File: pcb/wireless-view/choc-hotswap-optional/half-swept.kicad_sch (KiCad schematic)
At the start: 25 parts, among them J1 JST-BATTERY, SW1 SW_Push, SW10 SW_Push, SW11 SW_Push, SW12 SW_Push, SW13 SW_DPDT, SW14 SW_Push, SW15 SW_Push, SW16 SW_Push, SW17 SW_Push, SW18 SW_Push, SW2 SW_Push, SW20 SW_Push, SW21 SW_Push, SW3 SW_Push, SW4 SW_Push, SW5 SW_Push, SW6 SW_Push, SW7 SW_DPDT, SW8 SW_Push, SW9 SW_Push, U1 nice_nano

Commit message: updated wireless sweeeeeep to support mill-max as well
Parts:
- SW1, SW10, SW11, SW12, SW14, SW15, SW16, SW17, SW18, SW2, SW20, SW21, SW3, SW4, SW5, SW6, SW8, SW9: footprint fingerpunch:Kailh_socket_PG1350_optional_reversible -> fingerpunch:Kailh_socket_PG1350_optional_reversible_millmax

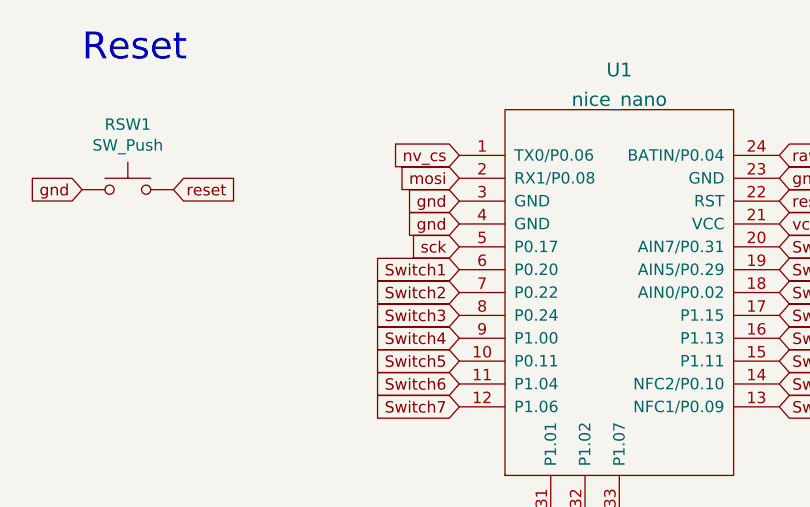
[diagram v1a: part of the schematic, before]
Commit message: Change n!n pin assigmnets to match ZMK's nice_view_adapter
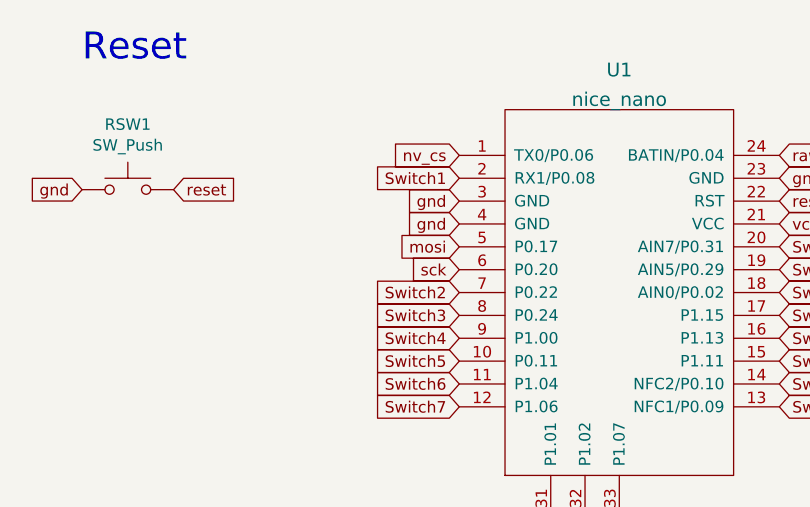
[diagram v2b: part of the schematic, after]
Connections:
- net Switch1: now also U1.2 (RX1/P0.08); no longer U1.6 (P0.20)
- net mosi: now also U1.5 (P0.17); no longer U1.2 (RX1/P0.08)
- net sck: now also U1.6 (P0.20); no longer U1.5 (P0.17)
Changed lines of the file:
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@@
     )
   )
-  (global_label "sck" (shape input) (at 158.75 45.72 180) (fields_autoplaced)
+  (global_label "sck" (shape input) (at 158.75 48.26 180) (fields_autoplaced)
     (effects (font (size 1.27 1.27)) (justify right))
-    (property "Intersheet References" "${INTERSHEET_REFS}" (id 0) (at 153.281 45.6406 0)
+    (property "Intersheet References" "${INTERSHEET_REFS}" (id 0) (at 153.281 48.1806 0)
       (effects (font (size 1.27 1.27)) (justify right) hide)
     )
@@
     )
   )
-  (global_label "Switch1" (shape input) (at 158.75 48.26 180) (fields_autoplaced)
+  (global_label "Switch1" (shape input) (at 158.75 38.1 180) (fields_autoplaced)
     (effects (font (size 1.27 1.27)) (justify right))
-    (property "Intersheet References" "${INTERSHEET_REFS}" (id 0) (at 0 -7.62 0)
+    (property "Intersheet References" "${INTERSHEET_REFS}" (id 0) (at 0 -17.78 0)
       (effects (font (size 1.27 1.27)) hide)
     )
@@
     )
   )
-  (global_label "mosi" (shape input) (at 158.75 38.1 180) (fields_autoplaced)
+  (global_label "mosi" (shape input) (at 158.75 45.72 180) (fields_autoplaced)
     (effects (font (size 1.27 1.27)) (justify right))
-    (property "Intersheet References" "${INTERSHEET_REFS}" (id 0) (at 151.9506 38.0206 0)
+    (property "Intersheet References" "${INTERSHEET_REFS}" (id 0) (at 151.9506 45.6406 0)
       (effects (font (size 1.27 1.27)) (justify right) hide)
     )
